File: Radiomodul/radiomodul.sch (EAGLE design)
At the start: 43 parts, among them IC1 MCP601R, IC2 AD5243, IC3 TXS0104, IC4 TXB0104PWR, IC5 NCV4274CSOT-223, IC6 E910.15, IC7 NCV4274CSOT-223, Q1 12MHz, U1 LPC1343FBD48, U2 MCP130T

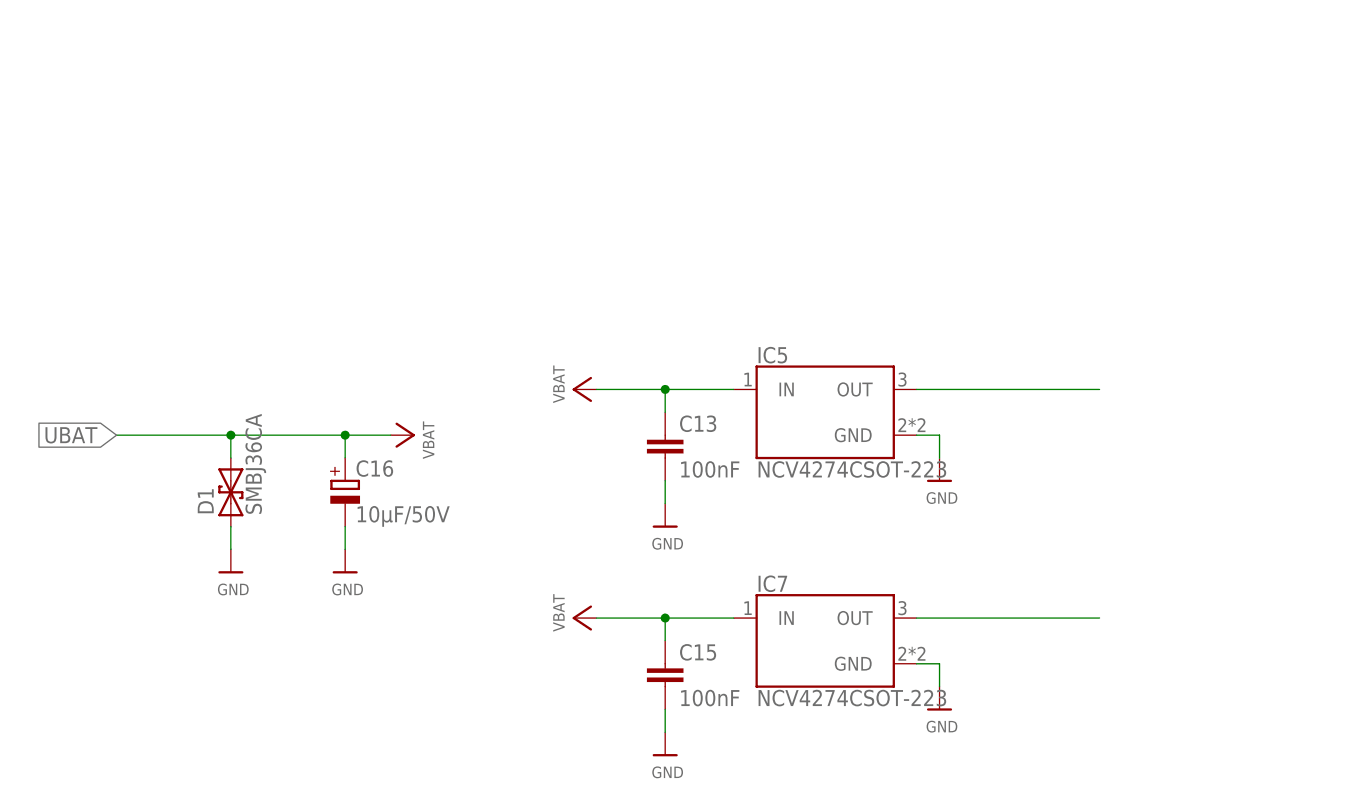
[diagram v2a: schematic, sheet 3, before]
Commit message: 
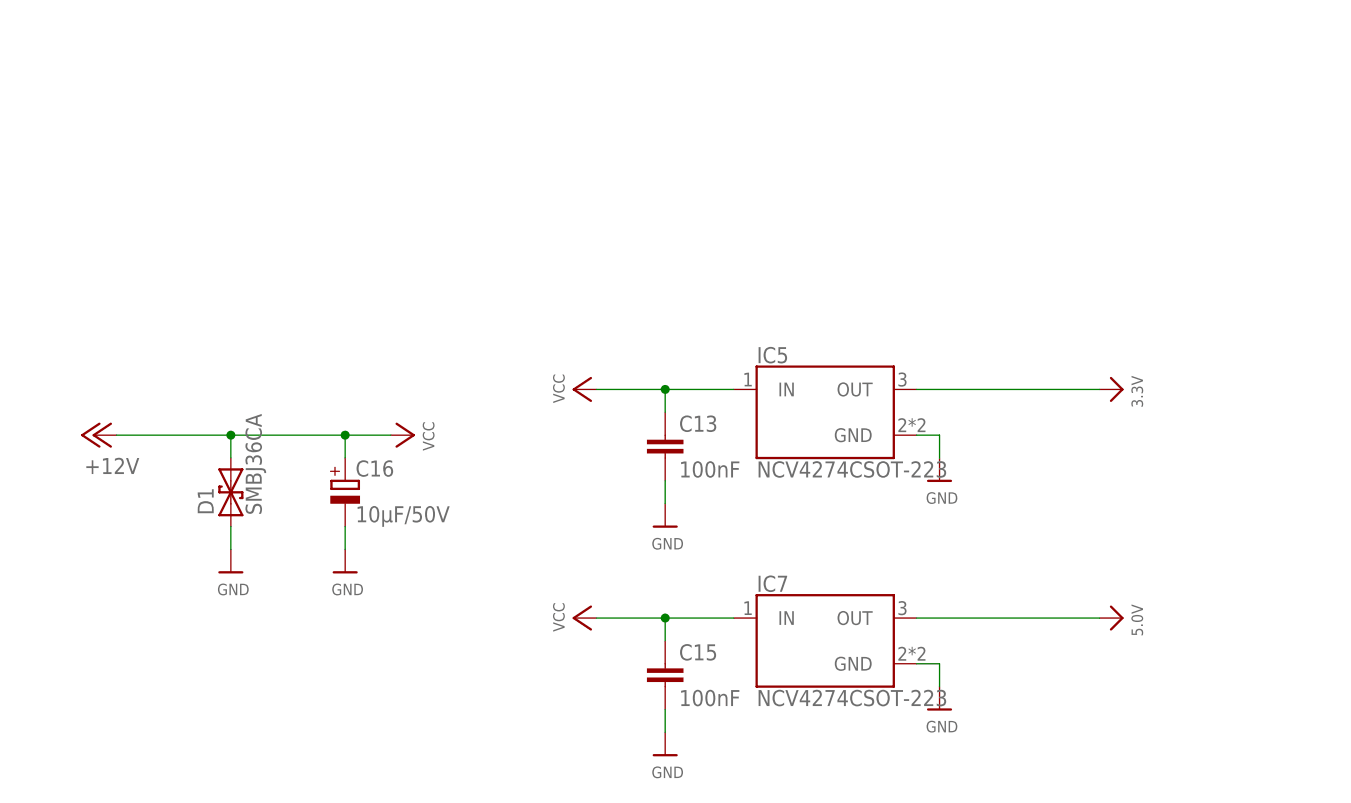
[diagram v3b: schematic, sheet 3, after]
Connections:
- net UBAT renamed +12V
- removed net N$11: IC7.OUT
- removed net N$12: IC5.OUT
- removed net VB: C19.1, D2.C, D4.C, IC6.VBAT
- new net VCC: C13.1, C15.1, D2.A, IC5.IN, IC7.IN
- net 3.3V: now also IC5.OUT
- net 5.0V: now also IC7.OUT
- net VBAT: now also C19.1, D2.C, D4.C, IC6.VBAT; no longer C13.1, C15.1, D2.A, IC5.IN, IC7.IN
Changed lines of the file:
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@@
 <part name="D1" library="Heinrich" deviceset="P6SMBXXCA" device="" value="SMBJ36CA"/>
 <part name="U$42" library="microbuilder" deviceset="GND" device=""/>
-<part name="U$43" library="microbuilder" deviceset="VBAT" device=""/>
-<part name="U$44" library="microbuilder" deviceset="VBAT" device=""/>
-<part name="U$45" library="microbuilder" deviceset="VBAT" device=""/>
 <part name="C16" library="rcl" library_urn="urn:adsk.eagle:library:334" deviceset="CPOL-EU" device="D" package3d_urn="urn:adsk.eagle:package:23424/2" value="10µF/50V"/>
 <part name="U$46" library="microbuilder" deviceset="GND" device=""/>
@@
 <part name="C19" library="rcl" library_urn="urn:adsk.eagle:library:334" deviceset="C-EU" device="C0805" package3d_urn="urn:adsk.eagle:package:23617/2" value="100nF"/>
 <part name="U$48" library="microbuilder" deviceset="GND" device=""/>
-<part name="U$49" library="microbuilder" deviceset="VBAT" device=""/>
+<part name="U$50" library="microbuilder" deviceset="3.3V" device=""/>
+<part name="U$51" library="microbuilder" deviceset="5.0V" device=""/>
+<part name="P+1" library="microbuilder" deviceset="VCC" device=""/>
+<part name="P+2" library="microbuilder" deviceset="VCC" device=""/>
+<part name="P+3" library="microbuilder" deviceset="VCC" device=""/>
+<part name="P+4" library="supply1" library_urn="urn:adsk.eagle:library:371" deviceset="+12V" device=""/>
+<part name="P+5" library="microbuilder" deviceset="VCC" device=""/>
 </parts>
 <sheets>
@@
 <instance part="D1" gate="G$1" x="27.94" y="101.6" rot="R90"/>
 <instance part="U$42" gate="G$1" x="27.94" y="93.98"/>
-<instance part="U$43" gate="G$1" x="45.72" y="109.22" rot="R270"/>
-<instance part="U$44" gate="G$1" x="68.58" y="114.3" rot="R90"/>
-<instance part="U$45" gate="G$1" x="68.58" y="88.9" rot="R90"/>
 <instance part="C16" gate="G$1" x="40.64" y="104.14"/>
 <instance part="U$46" gate="G$1" x="40.64" y="93.98"/>
+<instance part="U$50" gate="G$1" x="124.46" y="114.3" rot="R270"/>
+<instance part="U$51" gate="G$1" x="124.46" y="88.9" rot="R270"/>
+<instance part="P+1" gate="VCC" x="45.72" y="109.22" rot="R270"/>
+<instance part="P+2" gate="VCC" x="68.58" y="114.3" rot="R90"/>
+<instance part="P+3" gate="VCC" x="68.58" y="88.9" rot="R90"/>
+<instance part="P+4" gate="1" x="12.7" y="109.22" rot="R90"/>
 </instances>
 <busses>
@@
 </segment>
 </net>
-<net name="N$11" class="0">
+<net name="3.3V" class="0">
+<segment>
+<pinref part="IC5" gate="G$1" pin="OUT"/>
+<wire x1="104.14" y1="114.3" x2="124.46" y2="114.3" width="0.1524" layer="91"/>
+<pinref part="U$50" gate="G$1" pin="3.3V"/>
+</segment>
+</net>
+<net name="5.0V" class="0">
 <segment>
 <pinref part="IC7" gate="G$1" pin="OUT"/>
 <wire x1="104.14" y1="88.9" x2="124.46" y2="88.9" width="0.1524" layer="91"/>
-</segment>
-</net>
-<net name="N$12" class="0">
-<segment>
-<pinref part="IC5" gate="G$1" pin="OUT"/>
-<wire x1="104.14" y1="114.3" x2="124.46" y2="114.3" width="0.1524" layer="91"/>
-</segment>
-</net>
-<net name="VBAT" class="0">
+<pinref part="U$51" gate="G$1" pin="5.0V"/>
+</segment>
+</net>
+<net name="VCC" class="0">
 <segment>
 <pinref part="IC5" gate="G$1" pin="IN"/>
@@
 <wire x1="76.2" y1="111.76" x2="76.2" y2="114.3" width="0.1524" layer="91"/>
 <junction x="76.2" y="114.3"/>
-<pinref part="U$44" gate="G$1" pin="VBAT"/>
+<pinref part="P+2" gate="VCC" pin="VCC"/>
 </segment>
 <segment>
@@
 <wire x1="76.2" y1="88.9" x2="76.2" y2="86.36" width="0.1524" layer="91"/>
 <junction x="76.2" y="88.9"/>
-<pinref part="U$45" gate="G$1" pin="VBAT"/>
-</segment>
-</net>
-<net name="UBAT" class="0">
-<segment>
-<label x="15.24" y="109.22" size="1.778" layer="95" rot="R180" xref="yes"/>
+<pinref part="P+3" gate="VCC" pin="VCC"/>
+</segment>
+</net>
+<net name="+12V" class="0">
+<segment>
 <wire x1="15.24" y1="109.22" x2="27.94" y2="109.22" width="0.1524" layer="91"/>
 <pinref part="D1" gate="G$1" pin="2"/>
@@
 <wire x1="27.94" y1="106.68" x2="27.94" y2="109.22" width="0.1524" layer="91"/>
 <junction x="27.94" y="109.22"/>
-<pinref part="U$43" gate="G$1" pin="VBAT"/>
 <pinref part="C16" gate="G$1" pin="+"/>
 <wire x1="40.64" y1="106.68" x2="40.64" y2="109.22" width="0.1524" layer="91"/>
 <junction x="40.64" y="109.22"/>
+<pinref part="P+1" gate="VCC" pin="VCC"/>
+<pinref part="P+4" gate="1" pin="+12V"/>
 </segment>
 </net>
@@
 <instance part="C19" gate="G$1" x="78.74" y="91.44"/>
 <instance part="U$48" gate="G$1" x="78.74" y="81.28"/>
-<instance part="U$49" gate="G$1" x="104.14" y="96.52" rot="R270"/>
+<instance part="P+5" gate="VCC" x="104.14" y="96.52" rot="R270"/>
 </instances>
 <busses>
@@
 </segment>
 </net>
-<net name="VB" class="0">
-<segment>
-<pinref part="IC6" gate="G$1" pin="VBAT"/>
-<wire x1="139.7" y1="132.08" x2="149.86" y2="132.08" width="0.1524" layer="91"/>
-<label x="149.86" y="132.08" size="1.778" layer="95" xref="yes"/>
-</segment>
+<net name="VCC" class="0">
+<segment>
+<pinref part="D2" gate="G$1" pin="A"/>
+<wire x1="101.6" y1="96.52" x2="104.14" y2="96.52" width="0.1524" layer="91"/>
+<pinref part="P+5" gate="VCC" pin="VCC"/>
+</segment>
+</net>
+<net name="VBAT" class="0">
 <segment>
 <pinref part="D2" gate="G$1" pin="C"/>
@@
 <junction x="78.74" y="96.52"/>
 </segment>
-</net>
-<net name="VBAT" class="0">
-<segment>
-<pinref part="D2" gate="G$1" pin="A"/>
-<wire x1="101.6" y1="96.52" x2="104.14" y2="96.52" width="0.1524" layer="91"/>
-<pinref part="U$49" gate="G$1" pin="VBAT"/>
-</segment>
-</net>
+<segment>
+<pinref part="IC6" gate="G$1" pin="VBAT"/>
+<wire x1="139.7" y1="132.08" x2="149.86" y2="132.08" width="0.1524" layer="91"/>
+<label x="149.86" y="132.08" size="1.778" layer="95" xref="yes"/>
+</segment>
+</net>

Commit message: refactoring
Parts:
- added C20: 10µF, rcl:C-EUC1210
- added C21: 22µF, rcl:C-EUC1210
- added C22: 100nF, rcl:C-EUC0805
- C13, C15: device rcl:C-EUC0805 -> rcl:C-EUC1210
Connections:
- net R_BASE renamed R_SLEEVE
- net /SEN: now also U1.PIO0_7/!CTS!, U1.PIO2_1/!DSR!; no longer U1.PIO1_5/!RTS!/CT32B0_CAP0
- net 3.3V: now also C20.1
- net 5.0V: now also C21.1, C22.1
- net GND: now also C20.2, C21.2, C22.2
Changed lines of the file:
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@@
 <layer number="56" name="wert" color="7" fill="1" visible="no" active="no"/>
 <layer number="57" name="tCAD" color="7" fill="1" visible="no" active="no"/>
+<layer number="58" name="bCAD" color="11" fill="1" visible="no" active="no"/>
 <layer number="59" name="tPartCopper" color="7" fill="1" visible="no" active="no"/>
 <layer number="60" name="Board" color="7" fill="1" visible="no" active="no"/>
@@
 <part name="U$33" library="microbuilder" deviceset="GND" device=""/>
 <part name="U$34" library="microbuilder" deviceset="GND" device=""/>
-<part name="C13" library="rcl" library_urn="urn:adsk.eagle:library:334" deviceset="C-EU" device="C0805" package3d_urn="urn:adsk.eagle:package:23617/2" value="100nF"/>
-<part name="C15" library="rcl" library_urn="urn:adsk.eagle:library:334" deviceset="C-EU" device="C0805" package3d_urn="urn:adsk.eagle:package:23617/2" value="100nF"/>
+<part name="C13" library="rcl" library_urn="urn:adsk.eagle:library:334" deviceset="C-EU" device="C1210" package3d_urn="urn:adsk.eagle:package:23619/2" value="100nF"/>
+<part name="C15" library="rcl" library_urn="urn:adsk.eagle:library:334" deviceset="C-EU" device="C1210" package3d_urn="urn:adsk.eagle:package:23619/2" value="100nF"/>
 <part name="U$38" library="microbuilder" deviceset="GND" device=""/>
 <part name="U$41" library="microbuilder" deviceset="GND" device=""/>
@@
 <part name="P+4" library="supply1" library_urn="urn:adsk.eagle:library:371" deviceset="+12V" device=""/>
 <part name="P+5" library="microbuilder" deviceset="VCC" device=""/>
+<part name="C20" library="rcl" library_urn="urn:adsk.eagle:library:334" deviceset="C-EU" device="C1210" package3d_urn="urn:adsk.eagle:package:23619/2" value="10µF"/>
+<part name="C21" library="rcl" library_urn="urn:adsk.eagle:library:334" deviceset="C-EU" device="C1210" package3d_urn="urn:adsk.eagle:package:23619/2" value="22µF"/>
+<part name="U$43" library="microbuilder" deviceset="GND" device=""/>
+<part name="U$44" library="microbuilder" deviceset="GND" device=""/>
+<part name="C22" library="rcl" library_urn="urn:adsk.eagle:library:334" deviceset="C-EU" device="C0805" package3d_urn="urn:adsk.eagle:package:23617/2" value="100nF"/>
+<part name="U$45" library="microbuilder" deviceset="GND" device=""/>
 </parts>
 <sheets>
@@
 <segment>
 <pinref part="U1" gate="G$1" pin="PIO1_6/RXD/CT32B0_MAT0"/>
-<wire x1="129.54" y1="91.44" x2="144.78" y2="91.44" width="0.1524" layer="91"/>
-<label x="137.16" y="91.44" size="1.778" layer="95"/>
+<wire x1="129.54" y1="91.44" x2="139.7" y2="91.44" width="0.1524" layer="91"/>
+<label x="134.62" y="91.44" size="1.778" layer="95"/>
 </segment>
 </net>
@@
 <segment>
 <pinref part="U1" gate="G$1" pin="PIO1_7/TXD/CT32B0_MAT1"/>
-<wire x1="129.54" y1="88.9" x2="144.78" y2="88.9" width="0.1524" layer="91"/>
-<label x="137.16" y="88.9" size="1.778" layer="95"/>
-</segment>
-</net>
-<net name="/SEN" class="0">
-<segment>
-<pinref part="U1" gate="G$1" pin="PIO1_5/!RTS!/CT32B0_CAP0"/>
-<wire x1="129.54" y1="93.98" x2="144.78" y2="93.98" width="0.1524" layer="91"/>
-<label x="137.16" y="93.98" size="1.778" layer="95"/>
+<wire x1="129.54" y1="88.9" x2="139.7" y2="88.9" width="0.1524" layer="91"/>
+<label x="134.62" y="88.9" size="1.778" layer="95"/>
 </segment>
 </net>
@@
 <wire x1="35.56" y1="99.06" x2="20.32" y2="99.06" width="0.1524" layer="91"/>
 <label x="20.32" y="99.06" size="1.778" layer="95"/>
+</segment>
+</net>
+<net name="/SEN" class="0">
+<segment>
+<pinref part="U1" gate="G$1" pin="PIO0_7/!CTS!"/>
+<wire x1="35.56" y1="88.9" x2="20.32" y2="88.9" width="0.1524" layer="91"/>
+<label x="20.32" y="88.9" size="1.778" layer="95"/>
+</segment>
+<segment>
+<pinref part="U1" gate="G$1" pin="PIO2_1/!DSR!"/>
+<wire x1="129.54" y1="71.12" x2="139.7" y2="71.12" width="0.1524" layer="91"/>
+<label x="134.62" y="71.12" size="1.778" layer="95"/>
 </segment>
 </net>
@@
 </segment>
 </net>
-<net name="R_BASE" class="0">
+<net name="R_SLEEVE" class="0">
 <segment>
 <pinref part="IC2" gate="G$1" pin="W2"/>
@@
 <instance part="P+3" gate="VCC" x="68.58" y="88.9" rot="R90"/>
 <instance part="P+4" gate="1" x="12.7" y="109.22" rot="R90"/>
+<instance part="C20" gate="G$1" x="119.38" y="109.22"/>
+<instance part="C21" gate="G$1" x="119.38" y="83.82"/>
+<instance part="U$43" gate="G$1" x="119.38" y="99.06"/>
+<instance part="U$44" gate="G$1" x="119.38" y="73.66"/>
 </instances>
 <busses>
@@
 <pinref part="U$46" gate="G$1" pin="GND"/>
 </segment>
+<segment>
+<pinref part="C20" gate="G$1" pin="2"/>
+<pinref part="U$43" gate="G$1" pin="GND"/>
+<wire x1="119.38" y1="104.14" x2="119.38" y2="101.6" width="0.1524" layer="91"/>
+</segment>
+<segment>
+<pinref part="C21" gate="G$1" pin="2"/>
+<pinref part="U$44" gate="G$1" pin="GND"/>
+<wire x1="119.38" y1="78.74" x2="119.38" y2="76.2" width="0.1524" layer="91"/>
+</segment>
 </net>
 <net name="3.3V" class="0">
 <segment>
 <pinref part="IC5" gate="G$1" pin="OUT"/>
-<wire x1="104.14" y1="114.3" x2="124.46" y2="114.3" width="0.1524" layer="91"/>
+<wire x1="104.14" y1="114.3" x2="119.38" y2="114.3" width="0.1524" layer="91"/>
 <pinref part="U$50" gate="G$1" pin="3.3V"/>
+<pinref part="C20" gate="G$1" pin="1"/>
+<wire x1="119.38" y1="114.3" x2="124.46" y2="114.3" width="0.1524" layer="91"/>
+<wire x1="119.38" y1="111.76" x2="119.38" y2="114.3" width="0.1524" layer="91"/>
+<junction x="119.38" y="114.3"/>
 </segment>
 </net>
@@
 <segment>
 <pinref part="IC7" gate="G$1" pin="OUT"/>
-<wire x1="104.14" y1="88.9" x2="124.46" y2="88.9" width="0.1524" layer="91"/>
+<wire x1="104.14" y1="88.9" x2="119.38" y2="88.9" width="0.1524" layer="91"/>
 <pinref part="U$51" gate="G$1" pin="5.0V"/>
+<pinref part="C21" gate="G$1" pin="1"/>
+<wire x1="119.38" y1="88.9" x2="124.46" y2="88.9" width="0.1524" layer="91"/>
+<wire x1="119.38" y1="86.36" x2="119.38" y2="88.9" width="0.1524" layer="91"/>
+<junction x="119.38" y="88.9"/>
 </segment>
 </net>
@@
 <instance part="U$48" gate="G$1" x="78.74" y="81.28"/>
 <instance part="P+5" gate="VCC" x="104.14" y="96.52" rot="R270"/>
+<instance part="C22" gate="G$1" x="111.76" y="114.3"/>
+<instance part="U$45" gate="G$1" x="111.76" y="104.14"/>
 </instances>
 <busses>
@@
 <pinref part="U$48" gate="G$1" pin="GND"/>
 </segment>
+<segment>
+<pinref part="U$45" gate="G$1" pin="GND"/>
+<pinref part="C22" gate="G$1" pin="2"/>
+<wire x1="111.76" y1="106.68" x2="111.76" y2="109.22" width="0.1524" layer="91"/>
+</segment>
 </net>
 <net name="5.0V" class="0">
 <segment>
 <pinref part="IC6" gate="G$1" pin="VCC"/>
-<wire x1="114.3" y1="119.38" x2="104.14" y2="119.38" width="0.1524" layer="91"/>
+<wire x1="114.3" y1="119.38" x2="111.76" y2="119.38" width="0.1524" layer="91"/>
 <pinref part="U$36" gate="G$1" pin="5.0V"/>
-</segment>
-<segment>
+<pinref part="C22" gate="G$1" pin="1"/>
+<wire x1="111.76" y1="119.38" x2="104.14" y2="119.38" width="0.1524" layer="91"/>
+<wire x1="111.76" y1="116.84" x2="111.76" y2="119.38" width="0.1524" layer="91"/>
+<junction x="111.76" y="119.38"/>
+</segment>
+<segment>
